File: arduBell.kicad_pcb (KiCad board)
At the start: 2 copper layers, 60 x 60 mm, 48 parts, among them J1 AVR-ISP-6, J2 UART, J3 VCC, J4 BELL, J5 RELAY1, J6 RELAY2, Q1 BC548BTA, Q2 BC548BTA, SW1 SW_Push, SW2 SW_Push, U1 ATMEGA328P-AU, U2 NSL-32, Y1 Crystal_GND2

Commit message: 1st check
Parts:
- moved REF** 11.8 mm to (71.3, 62.1)
- moved REF** 11.8 mm to (71.4, 62.0)
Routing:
- net Net-(U1-Pad32): track 5.46 -> 0.00 mm
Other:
- board text added: "Made by Peter, DH2PP@eml.cc github.com/dh2pp/ardubell"
- board text removed: "Made by Peter DH2PP@eml.cc"

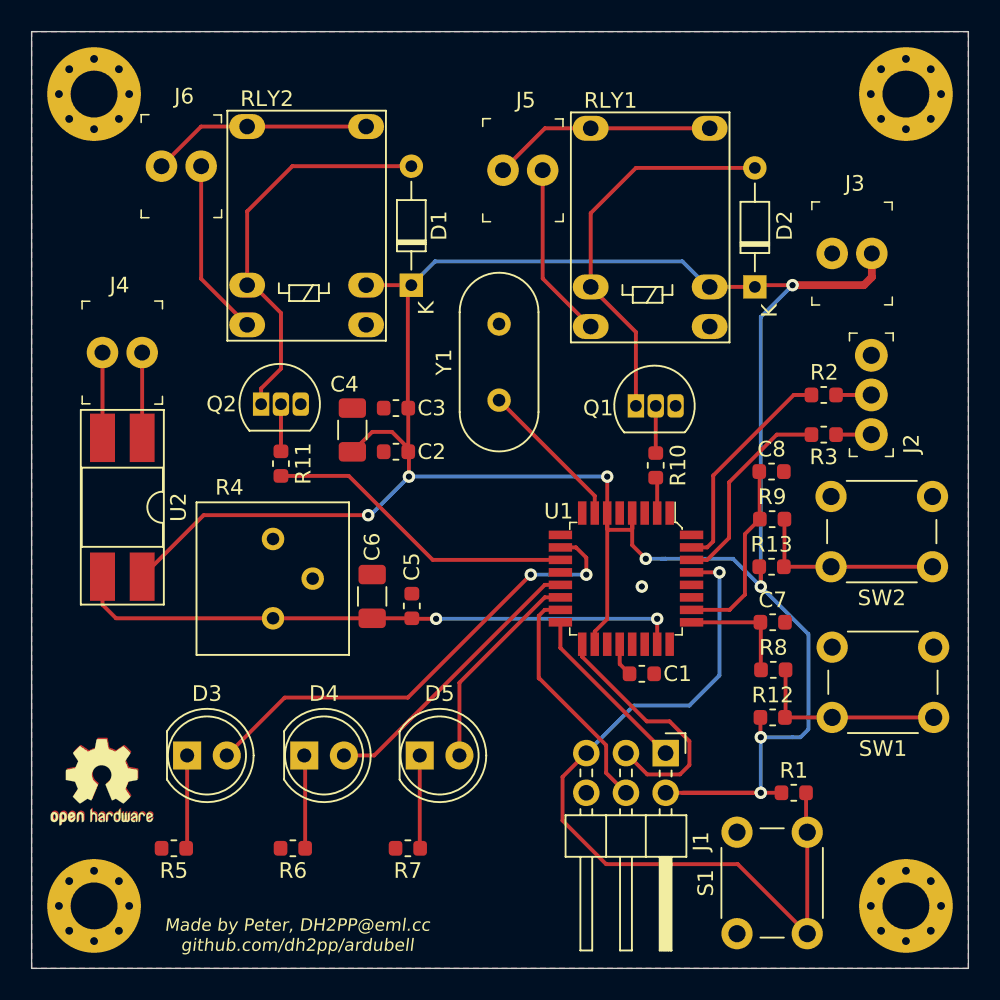
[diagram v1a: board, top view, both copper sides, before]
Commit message: rev 1a, XO fixed, more labels and rearranging
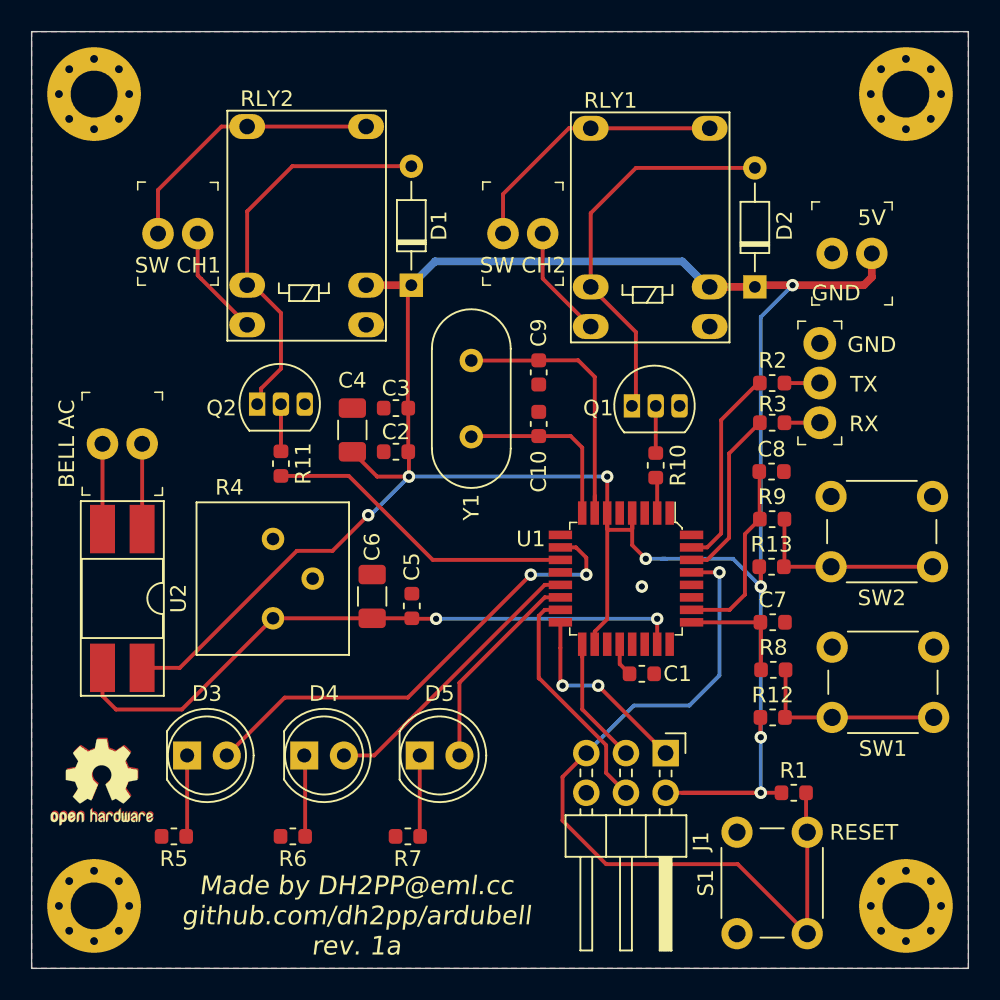
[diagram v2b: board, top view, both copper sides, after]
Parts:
- added C10: 10p, Capacitor_SMD:C_0603_1608Metric, F.Cu at (99.3, 39.1)
- added C9: 10p, Capacitor_SMD:C_0603_1608Metric, F.Cu at (99.3, 35.8)
- C1, C2, C5, C7, C8: value C_Small -> 100n
- C3: value C_Small -> 1u
- C4, C6: value CP_Small -> 4.7u
- R1, R12, R13, R2, R3, R8, R9: value R_Small -> 1K
- R5, R6, R7: value R_Small -> 100R
- Y1: value Crystal_GND2 -> Crystal
- moved J4 5.84 mm to (73.9, 40.4)
- moved U2 5.84 mm to (72.6, 50.3)
- moved J6 4.32 mm to (74.9, 26.9)
- moved J5 4.06 mm to (97.0, 26.9)
- moved J2 3.39 mm to (117.3, 39.0)
- moved R2 3.39 mm to (114.3, 36.5)
- moved R3 3.39 mm to (114.3, 39.0)
- moved Y1 3.10 mm to (95.0, 35.1), turned to 270 degrees
- moved R5 0.76 mm to (75.9, 65.5)
- moved R6 0.76 mm to (83.6, 65.5)
- moved R7 0.76 mm to (90.9, 65.5)
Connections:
- U1 pad 8: Net-(U1-Pad8) -> Net-(C10-Pad1)
- Y1 pad 2: GND -> Net-(C10-Pad1)
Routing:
- net Net-(C10-Pad1): track 0.00 -> 12.3 mm
- net Net-(C9-Pad1): track 9.77 -> 18.4 mm
- net SCK: track 16.3 -> 8.95 mm
- net /Relay 1/n_c: track 11.3 -> 6.97 mm
- net /Relay2/n_c: track 11.4 -> 7.15 mm
- net /Relay2/comm: track 14.2 -> 17.8 mm
- net /Relay 1/comm: track 14.3 -> 17.8 mm
- net /bell_detect: track 39.1 -> 41.5 mm
- net Net-(R3-Pad2): track 13.1 -> 11.2 mm
- net VCC: track 165.0 -> 163.2 mm
- net MISO: track 11.2 -> 12.5 mm, vias 0 -> 2
- net Net-(R2-Pad2): track 14.2 -> 13.0 mm
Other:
- board text added: "5V"
- board text added: "BELL AC"
- board text added: "GND"
- board text added: "Made by DH2PP@eml.cc github.com/dh2pp/ardubell rev. 1a"
- board text added: "RESET"
- board text added: "RX"
- board text added: "SW CH1"
- board text added: "SW CH2"
- board text added: "TX"
- board text removed: "Made by Peter, DH2PP@eml.cc github.com/dh2pp/ardubell"

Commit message: rev 1a: optocoupler works, quarz works
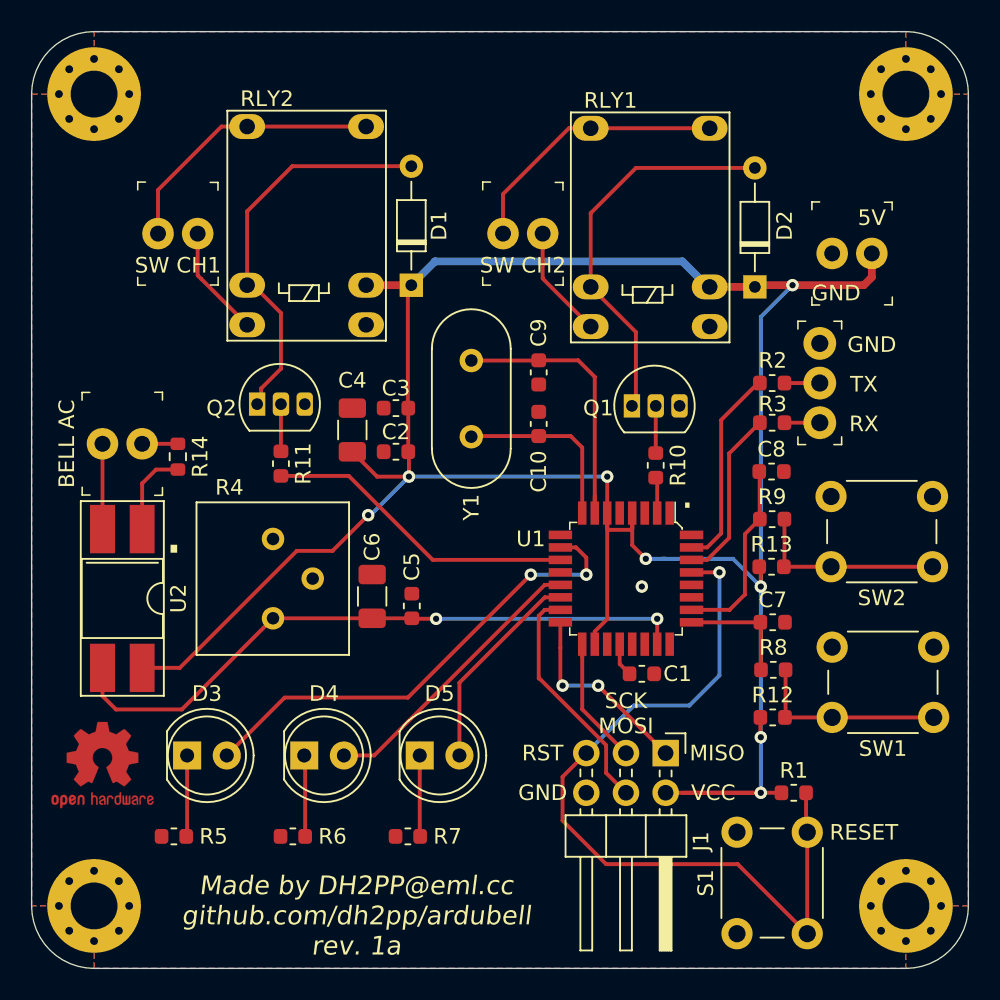
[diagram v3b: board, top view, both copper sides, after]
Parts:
- removed the REF** at (71.3, 62.1)
- added R14: 270R, Resistor_SMD:R_0603_1608Metric, F.Cu at (76.2, 41.2)
- added REF**: OSHW-Logo2_14.6x12mm_SilkScreen, Symbol:OSHW-Logo2_14.6x12mm_SilkScreen, B.Cu at (87.4, 67.8)
- moved REF** 1.02 mm to (71.4, 61.0)
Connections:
- U2 pad 1: Net-(J4-Pad1) -> Net-(R14-Pad2)
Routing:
- net Net-(R14-Pad2): track 0.00 -> 5.58 mm
- net Net-(J4-Pad1): track 5.71 -> 2.54 mm
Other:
- outline, holes or cut-outs redrawn
- board text added: "."
- board text added: "MISO"
- board text added: "RST"
- board text added: "SCK MOSI"
- board text added: "VCC"
